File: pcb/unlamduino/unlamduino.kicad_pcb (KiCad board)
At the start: 2 copper layers, 103.5 x 69.5 mm, 46 parts, among them IC2 ATMEGA328-P, P3 CONN_01X08, U1 LM2576, U2 AP111733, Y2 16MHz

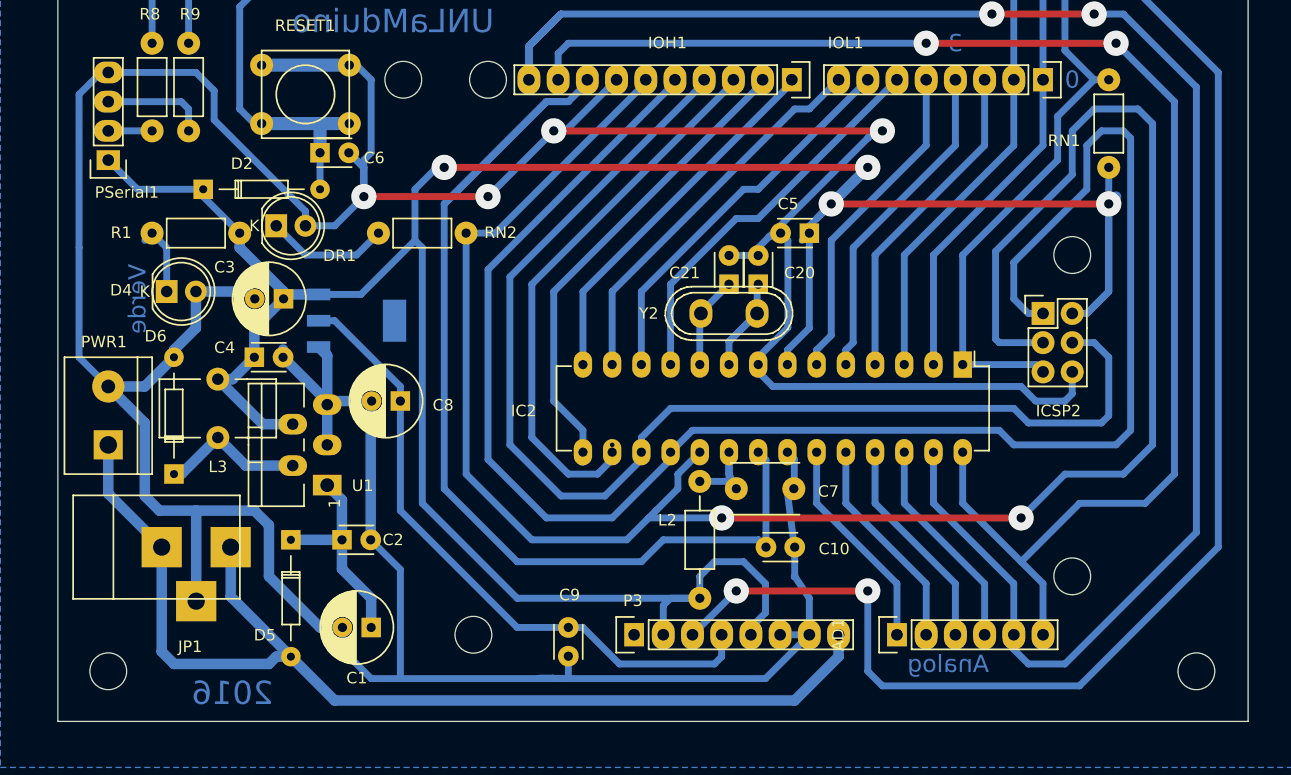
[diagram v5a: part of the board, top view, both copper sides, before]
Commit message: PCB Unlamduino: Muevo componentes para que no se superpomgam. Ubico L1 con su nuevo footprint. Subo o el margen a 0,5 mm. Corrijo varias pistas cerca. Aún pendientes C21, C20, L2, IOH1.
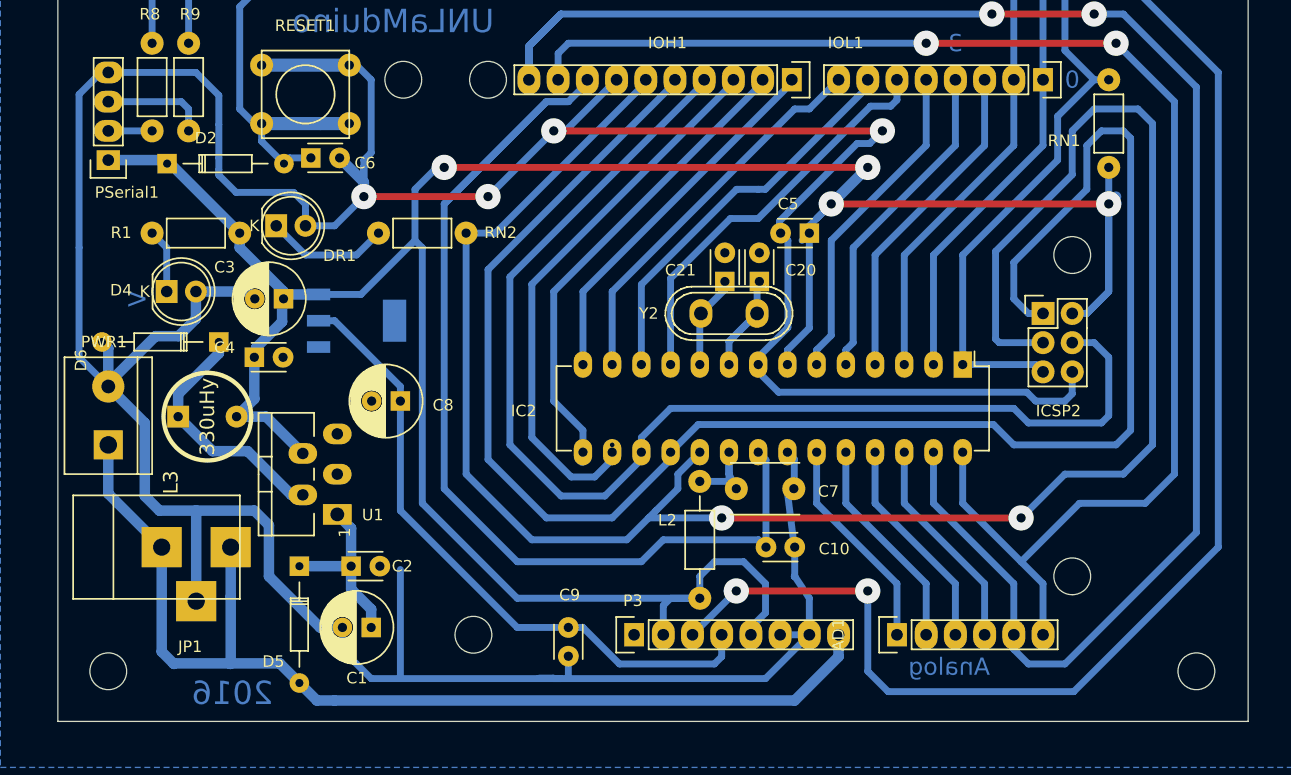
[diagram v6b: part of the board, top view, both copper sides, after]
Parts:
- L3: footprint Choke_Toroid_ThroughHole:Choke_Toroid_5x10mm_Vertical -> huellas:INDUCTOR_V
- moved D6 12.1 mm to (169.0, 75.5), turned to 180 degrees
- moved L3 4.55 mm to (168.0, 82.0)
- moved D2 3.85 mm to (164.5, 60.0)
- moved U1 2.69 mm to (175.5, 87.0)
- moved C2 2.42 mm to (180.5, 95.0)
- moved D5 2.41 mm to (176.0, 95.0)
- moved C6 0.92 mm to (177.0, 59.5)
- moved C21 0.43 mm to (213.0, 70.2)
- moved C20 0.26 mm to (216.0, 70.2)
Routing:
- net GND: track 394.3 -> 362.1 mm
- net Net-(D6-Pad1): track 12.7 -> 21.6 mm
- net Net-(C1-Pad1): track 18.1 -> 15.5 mm
- net /VIN: track 103.5 -> 101.6 mm
- net /RESET: track 263.0 -> 264.6 mm
- net /IO5: track 34.0 -> 35.4 mm
- net Net-(D4-Pad1): track 6.50 -> 5.61 mm
- net /IO6: track 33.7 -> 34.4 mm
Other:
- net class Default: clearance 0.2 -> 0.5
- rule trace_clearance: 0.2 -> 0.5
- board text added: "V"
- board text removed: "Verde"

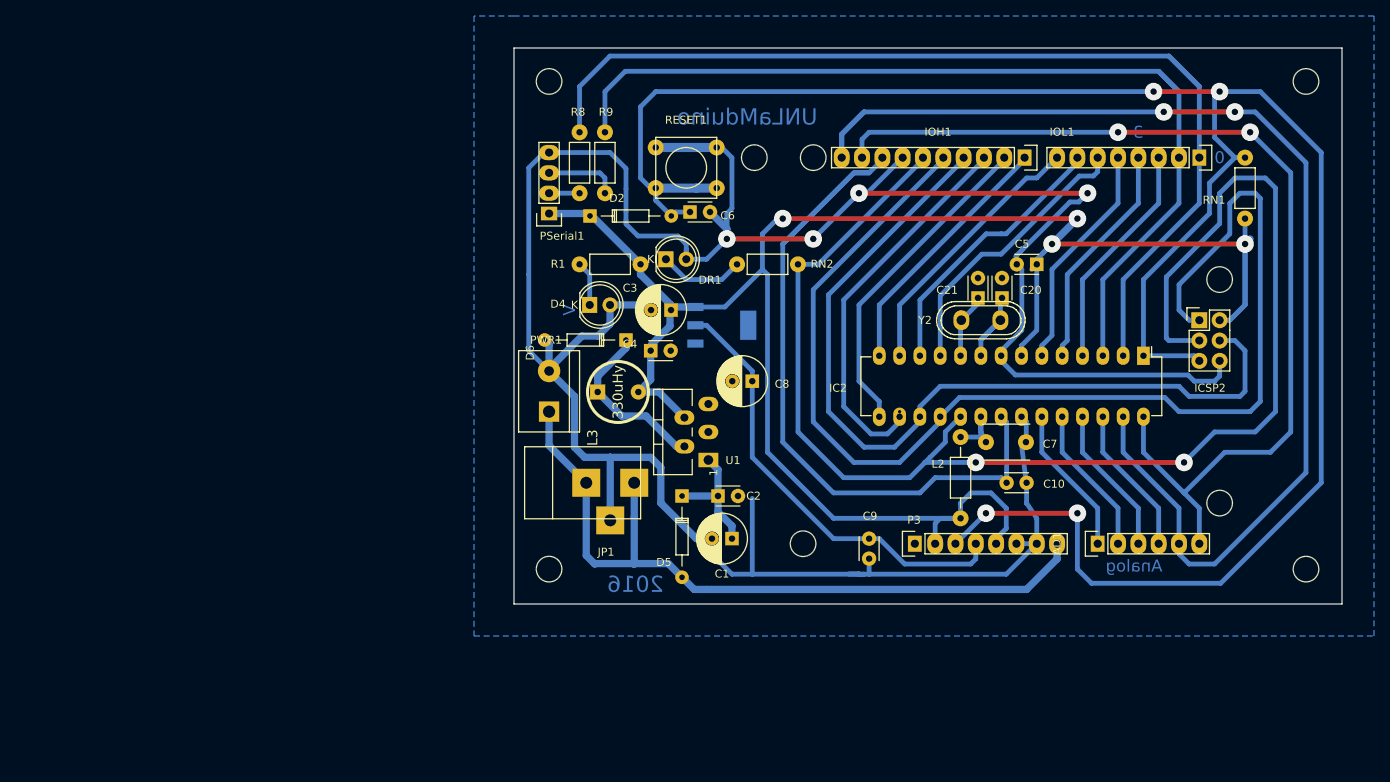
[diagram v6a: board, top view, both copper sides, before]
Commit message: Unlamduino pcb: Muevo los componentes superpuestos. Quito errores DRC para 0,5mm. Agrego textos y aclaraciones a la serigrafía.
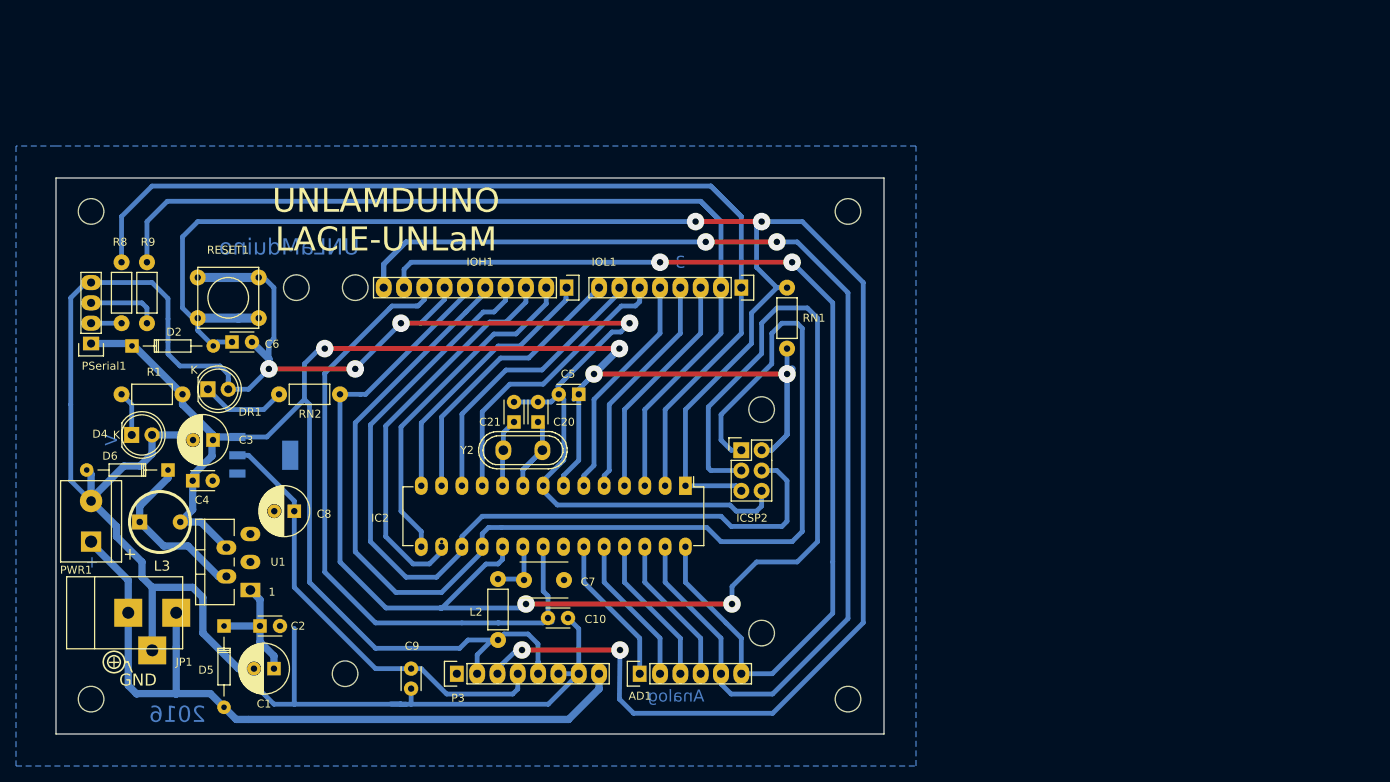
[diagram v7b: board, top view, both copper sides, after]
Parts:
- L2: footprint Resistors_ThroughHole:Resistor_Horizontal_RM10mm -> huellas:Resistor_Horizontal_RM7mm
- moved C7 60.3 mm to (156.2, 105.5)
- moved C20 60.0 mm to (158.0, 85.8)
- moved C21 60.0 mm to (155.0, 85.8)
- moved L2 59.8 mm to (153.0, 113.0)
- moved C10 59.8 mm to (161.8, 110.2)
- moved C4 59.5 mm to (114.8, 93.1)
- moved DR1 59.5 mm to (116.7, 81.7)
- moved JP1 59.5 mm to (106.6, 109.6)
- moved A1 59.5 mm to (196.8, 59.4)
- moved A2 59.5 mm to (196.8, 120.4)
- moved A6 59.5 mm to (135.2, 69.0)
- moved A7 59.5 mm to (186.0, 84.2)
- moved A8 59.5 mm to (133.9, 117.2)
- moved A9 59.5 mm to (186.0, 112.1)
- moved AD1 59.5 mm to (170.7, 117.2)
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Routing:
- net /AREF: track 97.8 -> 83.4 mm
- net GND: track 362.1 -> 354.7 mm
- net /IO13: track 177.3 -> 183.6 mm
- net +5V: track 245.7 -> 241.0 mm
- net /AD5/SCL: track 127.0 -> 131.5 mm
- net Net-(C7-Pad1): track 9.67 -> 7.65 mm
- net /IO9: track 42.2 -> 44.1 mm
- net /IO8: track 32.3 -> 34.1 mm
- net /IO6: track 34.4 -> 36.2 mm
- net /IO10: track 48.0 -> 49.5 mm
- net /IO7: track 33.7 -> 35.0 mm
- net /IO12: track 152.4 -> 153.6 mm
- net /AD4/SDA: track 165.3 -> 166.4 mm
- net /IO11: track 106.5 -> 107.5 mm
- net /IO5: track 35.4 -> 36.4 mm
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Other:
- board text added: "+"
- board text added: "GND"
- board text added: "UNLAMDUINO LACIE-UNLaM"
- board text removed: "0"

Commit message: Detalles de ruteo, serigrafía de borde de Arduino, Indicaciones en la serigrafía.
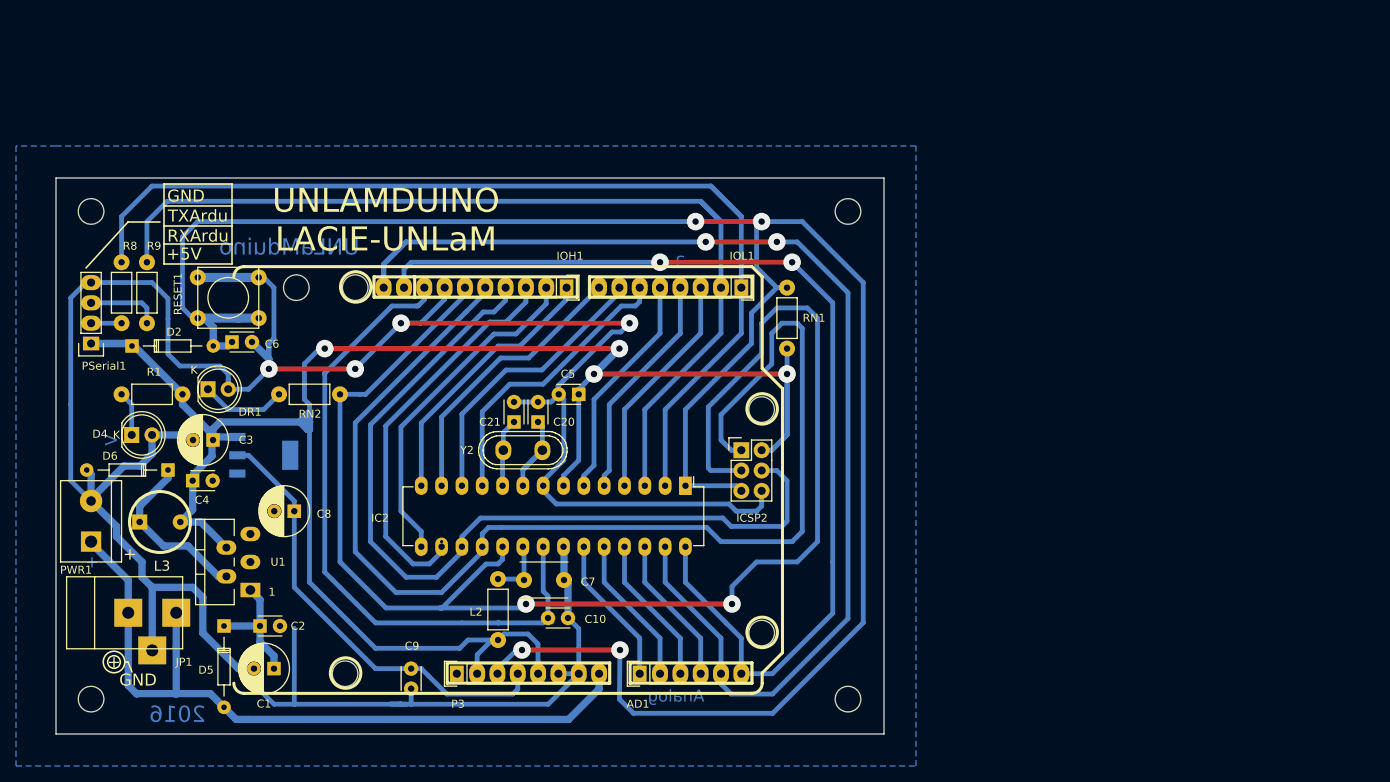
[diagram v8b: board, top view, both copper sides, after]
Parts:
- added Arduino_Borde: Val**, huellas:arduino_borde, F.Cu at (153.0, 93.0)
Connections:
- net Net-(PSerial1-Pad2) renamed /RXArdu
- net Net-(PSerial1-Pad3) renamed /TXArdu
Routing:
- net +5V: track 241.0 -> 253.6 mm
- net GND: track 354.7 -> 363.8 mm
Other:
- board text added: "+5V"
- board text added: "RXArdu"
- board text added: "TXArdu"
